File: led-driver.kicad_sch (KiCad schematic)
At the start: 6 parts, among them J30 LED1_Port, Q30 LBSS84LT1G, Q31 2N7002

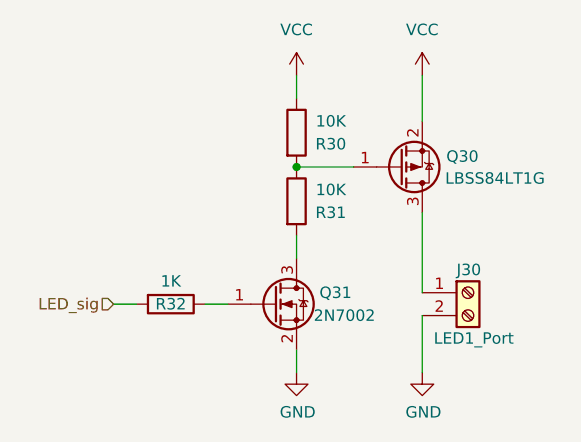
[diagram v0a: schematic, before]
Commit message: Initial board layout completed + initial routing started
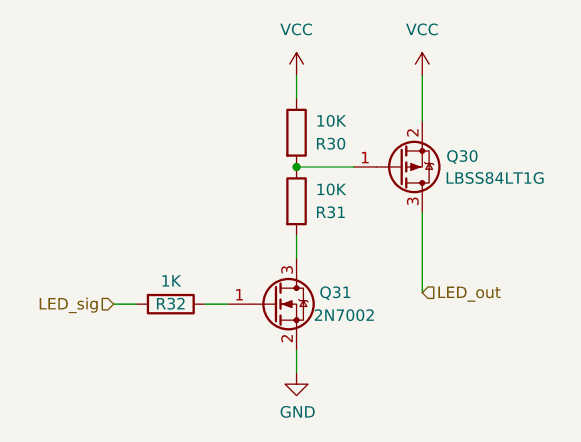
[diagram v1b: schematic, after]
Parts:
- removed J30: LED1_Port, AlfredoFootprints:TGD_ESC_SigPads, symbol Connector:Screw_Terminal_01x02
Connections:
- net LED_out: now reaches Q30.3 (D)
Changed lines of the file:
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@@
-    (stroke (width 0) (type default) (color 0 0 0 0))
-  )
-  (wire (pts (xy 153.67 113.03) (xy 153.67 119.38))
     (stroke (width 0) (type default) (color 0 0 0 0))
   )
@@
     (stroke (width 0) (type default) (color 0 0 0 0))
   )
+  (hierarchical_label "LED_out" (shape input) (at 153.67 110.49 0)
+    (effects (font (size 1.27 1.27)) (justify left))
+  )
   (hierarchical_label "LED_sig" (shape input) (at 119.38 111.76 180)
     (effects (font (size 1.27 1.27)) (justify right))
   )
-  (symbol (lib_id "Connector:Screw_Terminal_01x02") (at 158.75 110.49 0) (unit 1)
-    (in_bom yes) (on_board yes)
-    (property "Reference" "J30" (id 0) (at 157.48 107.95 0)
-      (effects (font (size 1.27 1.27)) (justify left))
-    )
-    (property "Value" "LED1_Port" (id 1) (at 154.94 115.57 0)
-      (effects (font (size 1.27 1.27)) (justify left))
-    )
-    (property "Footprint" "AlfredoFootprints:TGD_ESC_SigPads" (id 2) (at 158.75 110.49 0)
-      (effects (font (size 1.27 1.27)) hide)
-    )
-    (property "Datasheet" "~" (id 3) (at 158.75 110.49 0)
-      (effects (font (size 1.27 1.27)) hide)
-    )
-    (property "LCSC" "~" (id 4) (at 158.75 110.49 0)
-      (effects (font (size 1.27 1.27)) hide)
-    )
-    (pin "1")
-    (pin "2")
-  )
   (symbol (lib_id "power:VCC") (at 139.7 86.36 0) (unit 1)
     (in_bom yes) (on_board yes) (fields_autoplaced)
-    (property "Reference" "#PWR?" (id 0) (at 139.7 90.17 0)
+    (property "Reference" "#PWR0175" (id 0) (at 139.7 90.17 0)
       (effects (font (size 1.27 1.27)) hide)
     )
@@
     (pin "3")
   )
-  (symbol (lib_id "power:GND") (at 153.67 119.38 0) (unit 1)
-    (in_bom yes) (on_board yes)
-    (property "Reference" "#PWR?" (id 0) (at 153.67 125.73 0)
-      (effects (font (size 1.27 1.27)) hide)
-    )
-    (property "Value" "GND" (id 1) (at 153.797 123.7742 0))
-    (property "Footprint" "" (id 2) (at 153.67 119.38 0)
-      (effects (font (size 1.27 1.27)) hide)
-    )
-    (property "Datasheet" "" (id 3) (at 153.67 119.38 0)
-      (effects (font (size 1.27 1.27)) hide)
-    )
-    (pin "1")
-  )
   (symbol (lib_id "Device:R") (at 139.7 100.33 0) (unit 1)
     (in_bom yes) (on_board yes)
@@
   (symbol (lib_id "power:GND") (at 139.7 119.38 0) (unit 1)
     (in_bom yes) (on_board yes)
-    (property "Reference" "#PWR?" (id 0) (at 139.7 125.73 0)
+    (property "Reference" "#PWR0174" (id 0) (at 139.7 125.73 0)
       (effects (font (size 1.27 1.27)) hide)
     )
@@
   (symbol (lib_id "power:VCC") (at 153.67 86.36 0) (unit 1)
     (in_bom yes) (on_board yes) (fields_autoplaced)
-    (property "Reference" "#PWR?" (id 0) (at 153.67 90.17 0)
+    (property "Reference" "#PWR0176" (id 0) (at 153.67 90.17 0)
       (effects (font (size 1.27 1.27)) hide)
     )

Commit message: All LCSC components selected
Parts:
- R30, R31: LCSC ? -> C25744
- R32: LCSC ? -> C11702
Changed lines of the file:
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@@
       (effects (font (size 1.27 1.27)) hide)
     )
-    (property "Datasheet" "?" (id 3) (at 139.7 100.33 0)
+    (property "Datasheet" "https://lcsc.com/product-detail/Chip-Resistor---Surface-Mount_UNI-ROYALUniroyal-Elec-UNI-ROYALUniroyal-Elec-0402WGF1002TCE_C25744.html" (id 3) (at 139.7 100.33 0)
       (effects (font (size 1.27 1.27)) hide)
     )
-    (property "LCSC" "?" (id 4) (at 139.7 100.33 0)
+    (property "LCSC" "C25744" (id 4) (at 139.7 100.33 0)
       (effects (font (size 1.27 1.27)) hide)
     )
@@
       (effects (font (size 1.27 1.27)) hide)
     )
-    (property "Datasheet" "?" (id 3) (at 139.7 92.71 0)
+    (property "Datasheet" "https://lcsc.com/product-detail/Chip-Resistor---Surface-Mount_UNI-ROYALUniroyal-Elec-UNI-ROYALUniroyal-Elec-0402WGF1002TCE_C25744.html" (id 3) (at 139.7 92.71 0)
       (effects (font (size 1.27 1.27)) hide)
     )
-    (property "LCSC" "?" (id 4) (at 139.7 92.71 0)
+    (property "LCSC" "C25744" (id 4) (at 139.7 92.71 0)
       (effects (font (size 1.27 1.27)) hide)
     )
@@
       (effects (font (size 1.27 1.27)) hide)
     )
-    (property "Datasheet" "?" (id 3) (at 125.73 111.76 0)
+    (property "Datasheet" "https://lcsc.com/product-detail/Chip-Resistor---Surface-Mount_UNI-ROYALUniroyal-Elec-UNI-ROYALUniroyal-Elec-0402WGF1001TCE_C11702.html" (id 3) (at 125.73 111.76 0)
       (effects (font (size 1.27 1.27)) hide)
     )
-    (property "LCSC" "?" (id 4) (at 125.73 111.76 0)
+    (property "LCSC" "C11702" (id 4) (at 125.73 111.76 0)
       (effects (font (size 1.27 1.27)) hide)
     )
